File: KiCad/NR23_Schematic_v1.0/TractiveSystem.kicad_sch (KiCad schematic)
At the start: 22 parts, among them M1 Zero_7R_Motor

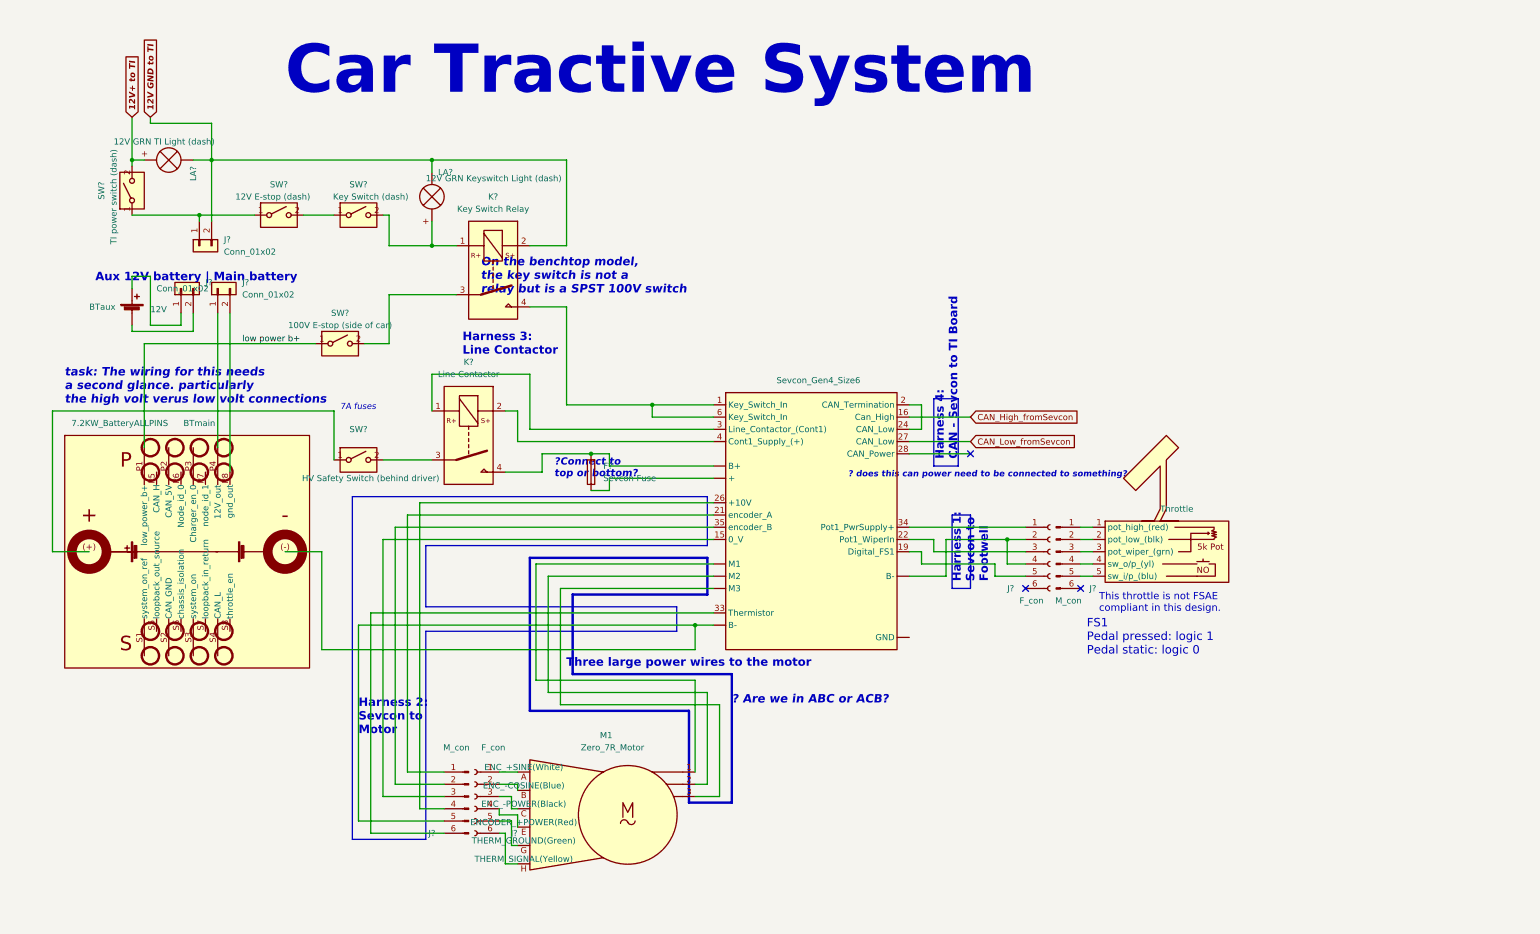
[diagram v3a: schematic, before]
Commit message: Added Dash to Schematic
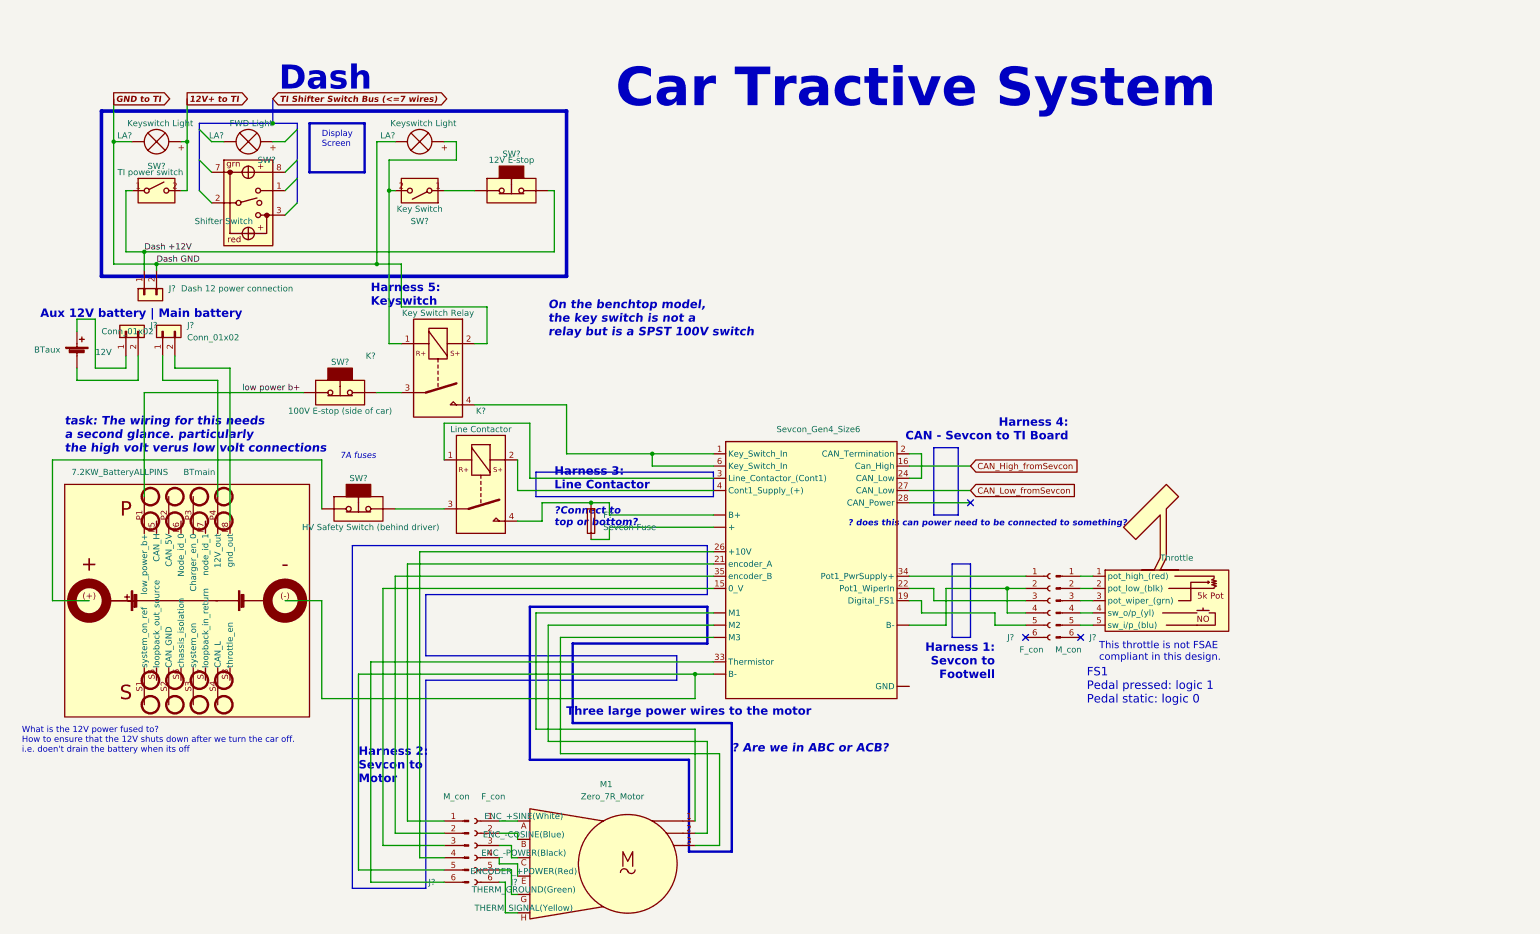
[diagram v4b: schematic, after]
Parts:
- removed J?: Conn_01x02, symbol Connector_Generic:Conn_01x02
- removed LA?: 12V GRN TI Light (dash), symbol Device:Lamp
- removed LA?: 12V GRN Keyswitch Light (dash), symbol Device:Lamp
- removed SW?: 12V E-stop (dash), symbol CamachosSymbols:SW_SPST
- removed SW?: TI power switch (dash), symbol CamachosSymbols:SW_SPST
- removed SW?: Key Switch (dash), symbol CamachosSymbols:SW_SPST
- added J?: Dash 12 power connection, symbol Connector_Generic:Conn_01x02
- added LA? (x2): Keyswitch Light, symbol Device:Lamp
- added LA?: FWD Light, symbol Device:Lamp
- added SW?: Key Switch, symbol CamachosSymbols:SW_SPST
- added SW?: 12V E-stop, symbol Switch:SW_Push_Open
- added SW?: TI power switch, symbol CamachosSymbols:SW_SPST
- added SW?: Shifter Switch, symbol CamachosSymbols:SW_SPDT_MSM
- SW? (x2): symbol CamachosSymbols:SW_SPST -> CamachosSymbols:Safety Switch
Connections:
- net 12V+ to TI: now also LA?.2 (+), SW?.2 (B)
- net at U?. (M3): now also J?.2 (Pin_2), J?.4 (Pin_4)
- net at K?.1: now also LA?.2 (+), SW?.2 (B)
- net 12V GND to TI renamed GND to TI
- net GND to TI: now also J?.2 (Pin_2), LA?.1 (-), LA?.1 (-)
- new net: SW?.1 (A), SW?.1 (A)
- new net Dash +12V: J?.1 (Pin_1), SW?.1 (A), SW?.2 (B)
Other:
- note added: "Dash"
- note added: "Display Screen"
- note added: "Harness 5: Keyswitch"
- note added: "What is the 12V power fused to? How to ensure that the 12V shuts down after we turn the car off. i.e. doen't drain the battery when its off"
- moved on the sheet: BTaux, BTmain, F?, J?, K?, M1

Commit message: worked some more on emergency stop switches
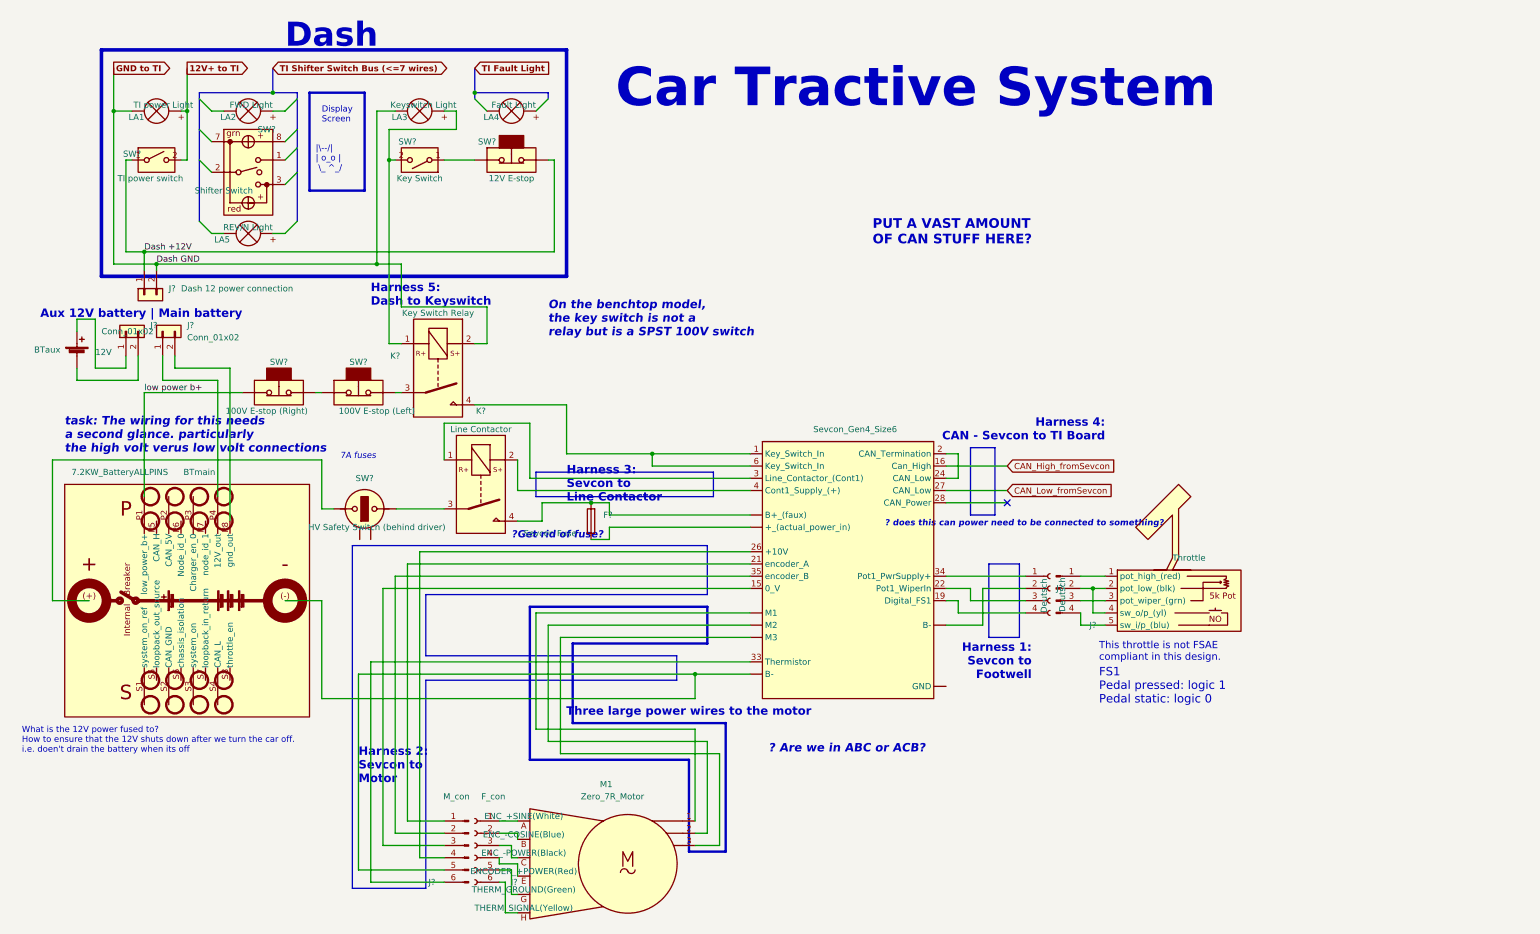
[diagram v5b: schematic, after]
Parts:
- removed J?: F_con, symbol Connector:Conn_01x06_Female
- added J?: Deutsch, symbol Connector:Conn_01x04_Female
- added LA4: Fault Light, symbol Device:Lamp
- added LA5: REV/N Light, symbol Device:Lamp
- added SW?: 100V E-stop (Right), symbol CamachosSymbols:Safety Switch
- J?: value M_con -> Deutsch; symbol Connector:Conn_01x06_Male -> Connector:Conn_01x04_Male
- LA1: renamed from LA?; value Keyswitch Light -> TI power Light
- SW?: value 100V E-stop (side of car) -> 100V E-stop (Left)
- gave numbers to parts that had none: 2
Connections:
- net low power b+: now also SW?.1 (A); no longer SW?.1 (A)
- net at J?.2 (Pin_2), U?.2 (pot_low_(blk)): now also U?.4 (sw_o/p_(yl))
- net at J?.4 (Pin_4): now also U?.5 (sw_i/p_(blu)); no longer U?.4 (sw_o/p_(yl))
- net at U?. (M3): now also F?.1
- net at U?.19 (Digital_FS1): now also J?.4 (Pin_4)
- net at U?.22 (Pot1_WiperIn): now also J?.3 (Pin_3)
- net at U?.34 (Pot1_PwrSupply+): now also J?.1 (Pin_1)
- new net: J?.2 (Pin_2), U?. (M3)
- new net: SW?.1 (A), SW?.2 (B)
- no-connect marks 3 -> 1
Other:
- note added: "?Get rid of fuse?"
- note added: "Harness 3: Sevcon to Line Contactor"
- note added: "Harness 5: Dash to Keyswitch"
- note added: "PUT A VAST AMOUNT OF CAN STUFF HERE?"
- note added: "|\--/| | o_o | \_ ^_/"
- note removed: "?Connect to top or bottom?"
- note removed: "Harness 3: Line Contactor"
- note removed: "Harness 5: Keyswitch"
- moved on the sheet: LA1, LA2, LA3, SW?

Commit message: added TI board box on the Tractive System Schematc
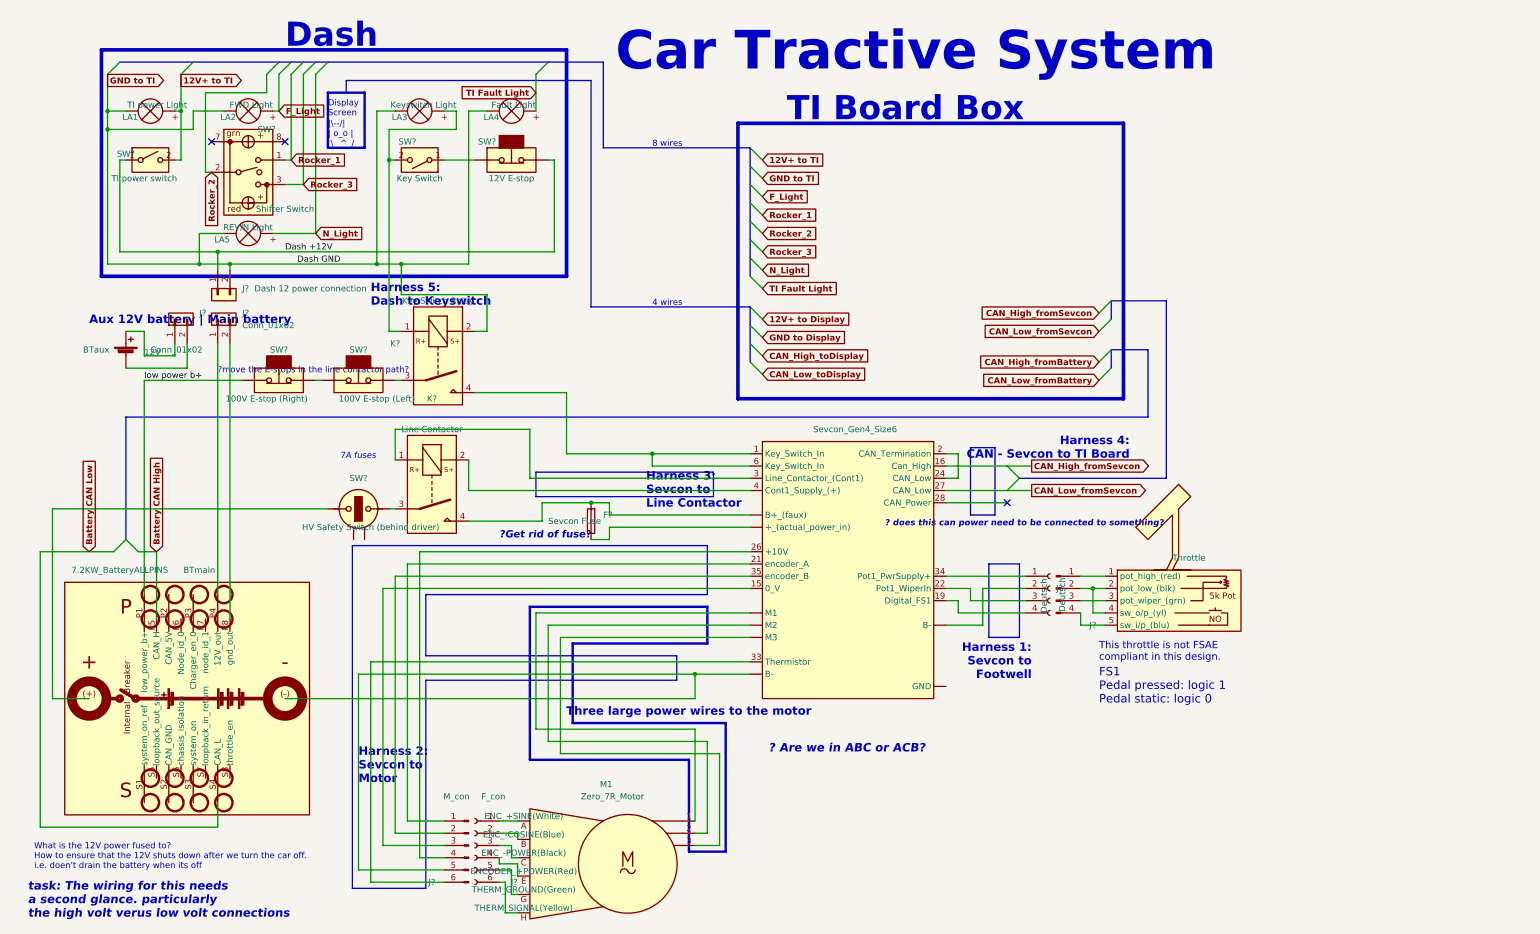
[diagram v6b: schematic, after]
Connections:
- net GND to TI: now also LA2.1 (-), LA4.1 (-), LA5.1 (-)
- net TI Fault Light: now also LA4.2 (+)
- net at U?. (M3): now also F?.1
- net F_Light: now reaches LA2.2 (+)
- net Rocker_1: now reaches SW?.1
- net Rocker_2: now reaches SW?.2
- net Rocker_3: now reaches SW?.3
- net Battery CAN High: now reaches BTmain.P5 (CAN_H)
- net Battery CAN Low: now reaches BTmain.S4 (CAN_L)
- net N_Light: now reaches LA5.2 (+)
- no-connect marks 1 -> 3
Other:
- note added: "4 wires"
- note added: "8 wires"
- note added: "?move the E-stops in the line contactor path?"
- note added: "TI Board Box"
- note removed: "On the benchtop model, the key switch is not a relay but is a SPST 100V switch"
- note removed: "PUT A VAST AMOUNT OF CAN STUFF HERE?"
- moved on the sheet: BTaux, BTmain, J?, K?, LA1, SW?

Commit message: endish of day 05APR23
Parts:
- added J?: Dash TI Connection, symbol Connector_Generic:Conn_02x06_Counter_Clockwise
- added J?: CAN Connector, symbol Connector_Generic:Conn_02x03_Counter_Clockwise
- added J? (x2): Dash Key Switch Connection, symbol Connector_Generic:Conn_01x02
- added J?: Display Connection, symbol Connector_Generic:Conn_02x06_Counter_Clockwise
- J?: value Conn_01x02 -> Dash 12 power connection
- J?: value Conn_01x02 -> Alt Dash 12 power connection
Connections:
- net 12V+ to Display: now also J?.1 (Pin_1)
- net 12V+ to TI: now also J?.6 (Pin_6)
- net CAN_High_fromBattery: now also J?.6 (Pin_6)
- net CAN_High_fromSevcon: now also J?.1 (Pin_1)
- net CAN_High_toDisplay: now also J?.10 (Pin_10)
- net CAN_Low_fromBattery: now also J?.5 (Pin_5)
- net CAN_Low_fromSevcon: now also J?.2 (Pin_2)
- net CAN_Low_toDisplay: now also J?.9 (Pin_9)
- net GND to Display: now also J?.2 (Pin_2)
- net GND to TI: now also J?.2 (Pin_2), J?.7 (Pin_7); no longer K?.2, LA2.1 (-), LA4.1 (-), LA5.1 (-)
- net Rocker_1: now also J?.12 (Pin_12)
- net Rocker_2: now also J?.11 (Pin_11)
- net Rocker_3: now also J?.1 (Pin_1)
- net at U?. (M3): now also F?.1
- net at U?.3 (Line_Contactor_(Cont1)): no longer K?.1
- net at U?.4 (Cont1_Supply_(+)): no longer K?.2
- net at LA3.2 (+), SW?.2 (B): now also J?.1 (Pin_1); no longer K?.1
- net at J?.1 (Pin_1): no longer BTmain.P4 (12V_out)
- net at J?.2 (Pin_2): no longer BTmain.P8 (gnd_out)
- net F_Light renamed F_Light(+)
- net F_Light(+): now also J?.2 (Pin_2)
- net N_Light renamed N_Light(+)
- net N_Light(+): now also J?.4 (Pin_4)
- net TI Fault Light renamed TI Fault Light(+)
- net TI Fault Light(+): now also J?.10 (Pin_10)
- new net: J?.1 (Pin_1), K?.1
- new net: J?.2 (Pin_2), K?.2
- new net Cont1 Supply (+): K?.2
- new net F_Light(-): J?.3 (Pin_3), LA2.1 (-)
- new net Line Contactor (Cont1): K?.1
- new net N_Light(-): J?.5 (Pin_5), LA5.1 (-)
- new net TI Fault Light(-): J?.9 (Pin_9), LA4.1 (-)
- no-connect marks 3 -> 5
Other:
- note added: "11 wires"
- note added: "?Get rid of F & N lights? ?Get rid of one of the rocker position pins?"
- note added: "?Where is the Key Switch Relay physically located?"
- note added: "?Where is the Line Contactor Relay physically located?"
- note added: "NEED HV ACTIVE LIGHT HERE ^"
- note added: "One hole in TI box -> for the CAN connections"
- note added: "Two holes in TI box for the dash connections ->"
- note removed: "7A fuses"
- note removed: "8 wires"
- note removed: "task: The wiring for this needs a second glance. particularly the high volt verus low volt connections"
- moved on the sheet: J?, LA1, LA2, LA3, LA4, LA5, SW?

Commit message: end of day 05APR23
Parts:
- removed F?: Sevcon Fuse, symbol Device:Fuse
- removed J?: Deutsch, symbol Connector:Conn_01x04_Male
- removed K?: Key Switch Relay, Relay_THT:Relay_1P1T_NO_10x24x18.8mm_Panasonic_ADW11xxxxW_THT, symbol Relay:ADW11
- removed K?: Line Contactor, Relay_THT:Relay_1P1T_NO_10x24x18.8mm_Panasonic_ADW11xxxxW_THT, symbol Relay:ADW11
- removed SW?: HV Safety Switch (behind driver), symbol CamachosSymbols:Safety Switch
- removed U?: Throttle, symbol CamachosSymbols:Throttle
- removed U?: Sevcon_Gen4_Size6, symbol CamachosSymbols:Sevcon_Gen4_Size6
- added F?: Sevcon Fuse, symbol Device:Fuse
- added J?: Deutsch, symbol Connector:Conn_01x04_Male
- added K?: Line Contactor, Relay_THT:Relay_1P1T_NO_10x24x18.8mm_Panasonic_ADW11xxxxW_THT, symbol Relay:ADW11
- added K?: Key Switch Relay, Relay_THT:Relay_1P1T_NO_10x24x18.8mm_Panasonic_ADW11xxxxW_THT, symbol Relay:ADW11
- added SW?: HV Safety Switch (behind driver), symbol CamachosSymbols:Safety Switch
- added U?: Throttle, symbol CamachosSymbols:Throttle
- added U?: Sevcon_Gen4_Size6, symbol CamachosSymbols:Sevcon_Gen4_Size6
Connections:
- net CAN_High_fromSevcon: now also U?.16 (Can_High)
- net CAN_Low_fromSevcon: now also U?.27 (CAN_Low)
- net Cont1 Supply (+): now also K?.2
- net Line Contactor (Cont1): now also K?.1
- net at M1.1: now also U?. (M3)
- net at M1.2: now also U?. (M3)
- net at M1.3: now also U?. (M3)
- net at BTmain.(-), J?.5 (Pin_5): now also U?. (M3)
- net at J?.2 (Pin_2): now also U?. (M3)
- net at J?.3 (Pin_3): now also U?.15 (0_V)
- net at J?.4 (Pin_4): now also U?.19 (Digital_FS1)
- net at J?.1 (Pin_1): now also U?.21 (encoder_A)
- net at J?.3 (Pin_3): now also U?.22 (Pot1_WiperIn)
- net at J?.4 (Pin_4): now also U?.26 (+10V)
- net at J?.6 (Pin_6): now also U?.33 (Thermistor)
- net at J?.1 (Pin_1): now also U?.34 (Pot1_PwrSupply+)
- net at J?.2 (Pin_2): now also U?.35 (encoder_B)
- net at BTmain.(+): now also SW?.1 (A)
- net at J?.1 (Pin_1): now also K?.1
- net at J?.2 (Pin_2): now also K?.2
- net at SW?.2 (B): now also K?.3
- new net: J?.1 (Pin_1), U?.1 (pot_high_(red))
- new net: J?.2 (Pin_2), U?.2 (pot_low_(blk)), U?.4 (sw_o/p_(yl))
- new net: J?.3 (Pin_3), U?.3 (pot_wiper_(grn))
- new net: J?.4 (Pin_4), U?.5 (sw_i/p_(blu))
- new net: F?.1, U?. (M3)
- new net: F?.2, K?.4, U?. (M3)
- new net: K?.4, U?.1 (Key_Switch_In), U?.6 (Key_Switch_In)
- new net: U?.2 (CAN_Termination), U?.24 (CAN_Low)
- new net: K?.3, SW?.2 (B)
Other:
- added sheet TI Schematic (Microcontroller.kicad_sch)
- note added: "CLICK RIGHT -> FOR DETAILED TI SCHEMATIC"
